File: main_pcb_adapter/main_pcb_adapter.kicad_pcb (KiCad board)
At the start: 2 copper layers, 20 x 25 mm, 3 parts, among them J1 DN, J2 UP, J3 UPDN

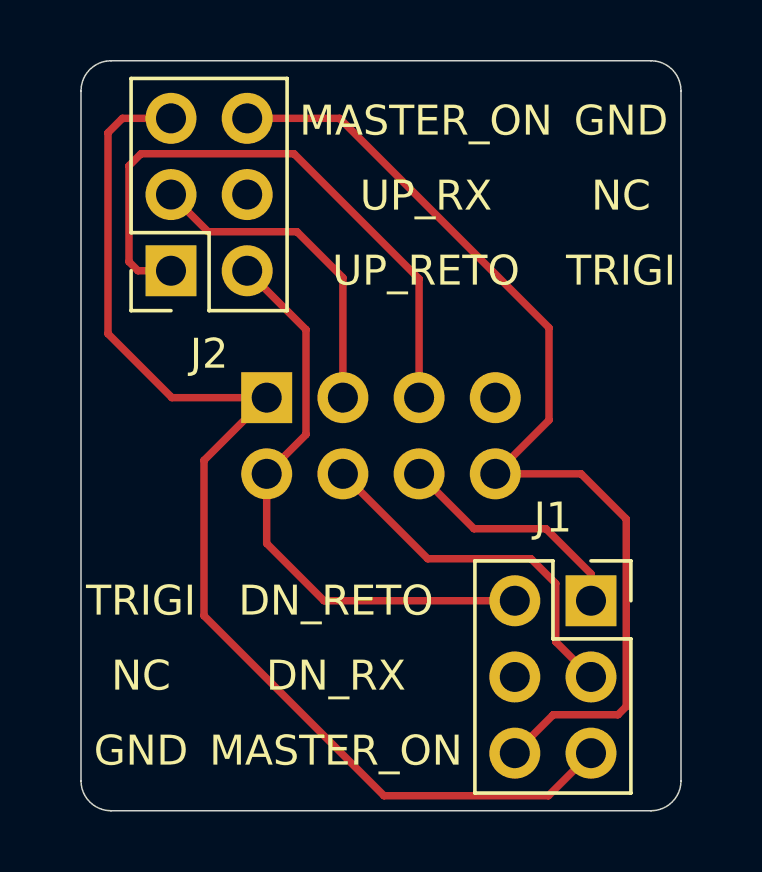
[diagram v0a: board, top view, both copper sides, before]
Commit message: Merged PCBs to KiCAD 6 format
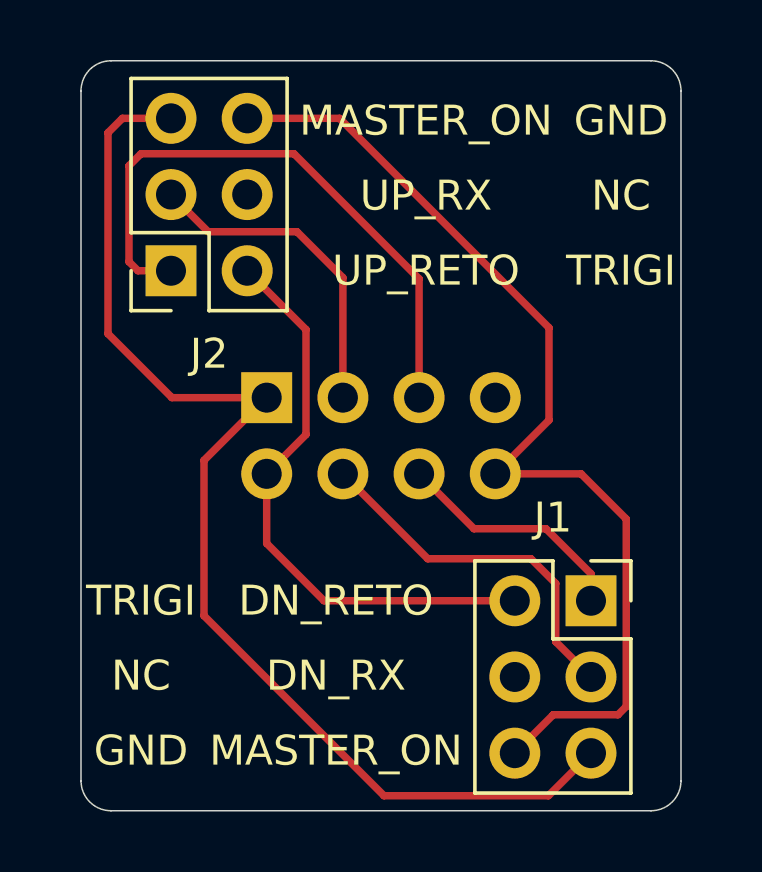
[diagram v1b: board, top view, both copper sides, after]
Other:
- net class Default removed
